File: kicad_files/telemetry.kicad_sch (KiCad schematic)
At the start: 24 parts, among them J5 SM10B-GHS-TB, J6 Conn_ARM_JTAG_SWD_10, J7 RFD900ux 3 Pin Power Select, J8 USB_C_Receptacle_USB2.0_16P, U8 74LVC1G125, U9 WE-TVS-82400102

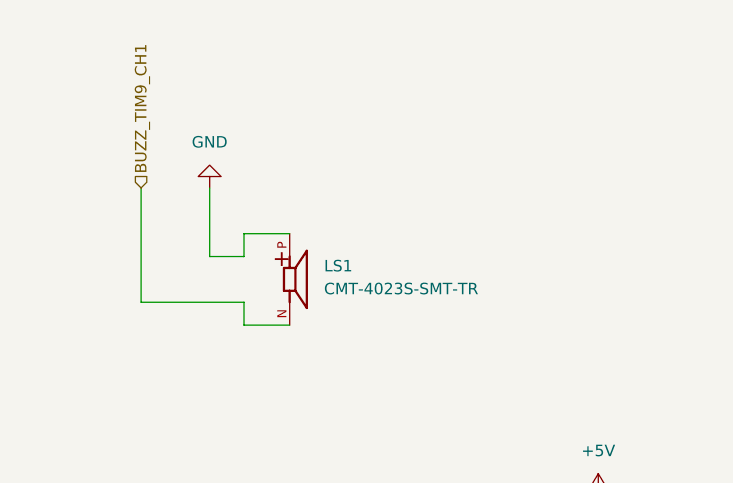
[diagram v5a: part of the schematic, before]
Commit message: fix buzzer
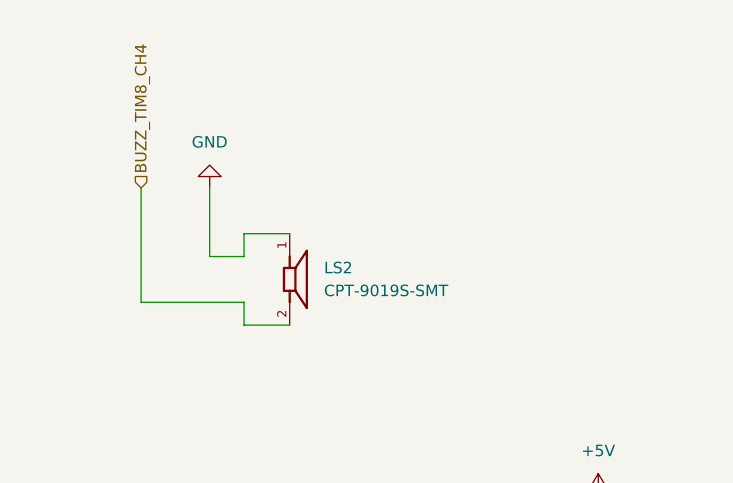
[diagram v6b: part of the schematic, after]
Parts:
- removed LS1: CMT-4023S-SMT-TR, footprints:CUI_CMT-4023S-SMT-TR, symbol CMT-4023S-SMT-TR:CMT-4023S-SMT-TR
- added LS2: CPT-9019S-SMT, footprints:CUI_CPT-9019S-SMT, symbol CPT-9019S-SMT:CPT-9019S-SMT
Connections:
- net GND: now also LS2.1
- new net BUZZ_TIM8_CH4: LS2.2
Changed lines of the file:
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@@
 		)
 	)
+	(hierarchical_label "BUZZ_TIM8_CH4"
+		(shape input)
+		(at 29.21 36.83 90)
+		(effects
+			(font
+				(size 1.27 1.27)
+			)
+			(justify left)
+		)
+	)
 	(hierarchical_label "RADIO_GPIO"
 		(shape input)
@@
 		)
 	)
-	(hierarchical_label "BUZZ_TIM9_CH1"
-		(shape input)
-		(at 29.21 36.83 90)
-		(effects
-			(font
-				(size 1.27 1.27)
-			)
-			(justify left)
-		)
-	)
 	(hierarchical_label "USART3_TX_RADIO"
 		(shape input)
@@
 	)
 	(symbol
+		(lib_id "CPT-9019S-SMT:CPT-9019S-SMT")
+		(at 45.72 46.99 0)
+		(unit 1)
+		(body_style 1)
+		(exclude_from_sim no)
+		(in_bom yes)
+		(on_board yes)
+		(in_pos_files yes)
+		(dnp no)
+		(fields_autoplaced yes)
+		(property "Reference" "LS2"
+			(at 49.53 45.7199 0)
+			(show_name no)
+			(do_not_autoplace no)
+			(effects
+				(font
+					(size 1.27 1.27)
+				)
+				(justify left)
+			)
+		)
+		(property "Value" "CPT-9019S-SMT"
+			(at 49.53 48.2599 0)
+			(show_name no)
+			(do_not_autoplace no)
+			(effects
+				(font
+					(size 1.27 1.27)
+				)
+				(justify left)
+			)
+		)
+		(property "Footprint" "footprints:CUI_CPT-9019S-SMT"
+			(at 45.72 46.99 0)
+			(hide yes)
+			(show_name no)
+			(do_not_autoplace no)
+			(effects
+				(font
+					(size 1.27 1.27)
+				)
+				(justify bottom)
+			)
+		)
+		(property "Datasheet" ""
+			(at 45.72 46.99 0)
+			(hide yes)
+			(show_name no)
+			(do_not_autoplace no)
+			(effects
+				(font
+					(size 1.27 1.27)
+				)
+			)
+		)
+		(property "Description" "9 mm, 25 Vp-p Vdc, 65 dB, Surface Mount (SMT), Piezo Audio Transducer Buzzer"
+			(at 45.72 46.99 0)
+			(hide yes)
+			(show_name no)
+			(do_not_autoplace no)
+			(effects
+				(font
+					(size 1.27 1.27)
+				)
+				(justify bottom)
+			)
+		)
+		(property "MF" "Same Sky"
+			(at 45.72 46.99 0)
+			(hide yes)
+			(show_name no)
+			(do_not_autoplace no)
+			(effects
+				(font
+					(size 1.27 1.27)
+				)
+				(justify bottom)
+			)
+		)
+		(property "Package" "None"
+			(at 45.72 46.99 0)
+			(hide yes)
+			(show_name no)
+			(do_not_autoplace no)
+			(effects
+				(font
+					(size 1.27 1.27)
+				)
+				(justify bottom)
+			)
+		)
+		(property "Price" "None"
+			(at 45.72 46.99 0)
+			(hide yes)
+			(show_name no)
+			(do_not_autoplace no)
+			(effects
+				(font
+					(size 1.27 1.27)
+				)
+				(justify bottom)
+			)
+		)
+		(property "Check_prices" "https://www.snapeda.com/parts/CPT-9019S-SMT-TR/Same+Sky/view-part/?ref=eda"
+			(at 45.72 46.99 0)
+			(hide yes)
+			(show_name no)
+			(do_not_autoplace no)
+			(effects
+				(font
+					(size 1.27 1.27)
+				)
+				(justify bottom)
+			)
+		)
+		(property "PART_REV" "1.0"
+			(at 45.72 46.99 0)
+			(hide yes)
+			(show_name no)
+			(do_not_autoplace no)
+			(effects
+				(font
+					(size 1.27 1.27)
+				)
+				(justify bottom)
+			)
+		)
+		(property "STANDARD" "MANUFACTURER RECOMMENDATIONS"
+			(at 45.72 46.99 0)
+			(hide yes)
+			(show_name no)
+			(do_not_autoplace no)
+			(effects
+				(font
+					(size 1.27 1.27)
+				)
+				(justify bottom)
+			)
+		)
+		(property "SnapEDA_Link" "https://www.snapeda.com/parts/CPT-9019S-SMT-TR/Same+Sky/view-part/?ref=snap"
+			(at 45.72 46.99 0)
+			(hide yes)
+			(show_name no)
+			(do_not_autoplace no)
+			(effects
+				(font
+					(size 1.27 1.27)
+				)
+				(justify bottom)
+			)
+		)
+		(property "MP" "CPT-9019S-SMT-TR"
+			(at 45.72 46.99 0)
+			(hide yes)
+			(show_name no)
+			(do_not_autoplace no)
+			(effects
+				(font
+					(size 1.27 1.27)
+				)
+				(justify bottom)
+			)
+		)
+		(property "Availability" "In Stock"
+			(at 45.72 46.99 0)
+			(hide yes)
+			(show_name no)
+			(do_not_autoplace no)
+			(effects
+				(font
+					(size 1.27 1.27)
+				)
+				(justify bottom)
+			)
+		)
+		(property "MANUFACTURER" "CUI INC"
+			(at 45.72 46.99 0)
+			(hide yes)
+			(show_name no)
+			(do_not_autoplace no)
+			(effects
+				(font
+					(size 1.27 1.27)
+				)
+				(justify bottom)
+			)
+		)
+		(pin "1"
+		)
+		(pin "2"
+		)
+		(instances
+			(project "versorlite"
+				(path "/1a230af0-0a74-48f7-8607-b087121dda49/4d884b5c-b332-4347-90a4-1c2e65497882"
+					(reference "LS2")
+					(unit 1)
+				)
+			)
+		)
+	)
+	(symbol
 		(lib_id "Connector:USB_C_Receptacle_USB2.0_16P")
 		(at 201.93 82.55 0)
@@
 					(unit 1)
 				)
-			)
-		)
-	)
-	(symbol
-		(lib_id "CMT-4023S-SMT-TR:CMT-4023S-SMT-TR")
-		(at 45.72 46.99 0)
-		(unit 1)
-		(body_style 1)
-		(exclude_from_sim no)
-		(in_bom yes)
-		(on_board yes)
-		(in_pos_files yes)
-		(dnp no)
-		(fields_autoplaced yes)
-		(property "Reference" "LS1"
-			(at 49.53 45.5097 0)
-			(show_name no)
-			(do_not_autoplace no)
-			(effects
-				(font
-					(size 1.27 1.27)
-				)
-				(justify left)
-			)
-		)
-		(property "Value" "CMT-4023S-SMT-TR"
-			(at 49.53 48.0497 0)
-			(show_name no)
-			(do_not_autoplace no)
-			(effects
-				(font
-					(size 1.27 1.27)
-				)
-				(justify left)
-			)
-		)
-		(property "Footprint" "footprints:CUI_CMT-4023S-SMT-TR"
-			(at 45.72 46.99 0)
-			(hide yes)
-			(show_name no)
-			(do_not_autoplace no)
-			(effects
-				(font
-					(size 1.27 1.27)
-				)
-				(justify bottom)
-			)
-		)
-		(property "Datasheet" ""
-			(at 45.72 46.99 0)
-			(hide yes)
-			(show_name no)
-			(do_not_autoplace no)
-			(effects
-				(font
-					(size 1.27 1.27)
-				)
-			)
-		)
-		(property "Description" "4 mm, 3 Vo-p, 70 dB, Surface Mount (SMT), Magnetic Audio Transducer Buzzer"
-			(at 45.72 46.99 0)
-			(hide yes)
-			(show_name no)
-			(do_not_autoplace no)
-			(effects
-				(font
-					(size 1.27 1.27)
-				)
-				(justify bottom)
-			)
-		)
-		(property "MF" "Same Sky"
-			(at 45.72 46.99 0)
-			(hide yes)
-			(show_name no)
-			(do_not_autoplace no)
-			(effects
-				(font
-					(size 1.27 1.27)
-				)
-				(justify bottom)
-			)
-		)
-		(property "Package" "None"
-			(at 45.72 46.99 0)
-			(hide yes)
-			(show_name no)
-			(do_not_autoplace no)
-			(effects
-				(font
-					(size 1.27 1.27)
-				)
-				(justify bottom)
-			)
-		)
-		(property "Price" "None"
-			(at 45.72 46.99 0)
-			(hide yes)
-			(show_name no)
-			(do_not_autoplace no)
-			(effects
-				(font
-					(size 1.27 1.27)
-				)
-				(justify bottom)
-			)
-		)
-		(property "Check_prices" "https://www.snapeda.com/parts/CMT-4023S-SMT-TR/Same+Sky/view-part/?ref=eda"
-			(at 45.72 46.99 0)
-			(hide yes)
-			(show_name no)
-			(do_not_autoplace no)
-			(effects
-				(font
-					(size 1.27 1.27)
-				)
-				(justify bottom)
-			)
-		)
-		(property "STANDARD" "Manufacturer recommendations"
-			(at 45.72 46.99 0)
-			(hide yes)
-			(show_name no)
-			(do_not_autoplace no)
-			(effects
-				(font
-					(size 1.27 1.27)
-				)
-				(justify bottom)
-			)
-		)
-		(property "PARTREV" "1.0"
-			(at 45.72 46.99 0)
-			(hide yes)
-			(show_name no)
-			(do_not_autoplace no)
-			(effects
-				(font
-					(size 1.27 1.27)
-				)
-				(justify bottom)
-			)
-		)
-		(property "SnapEDA_Link" "https://www.snapeda.com/parts/CMT-4023S-SMT-TR/Same+Sky/view-part/?ref=snap"
-			(at 45.72 46.99 0)
-			(hide yes)
-			(show_name no)
-			(do_not_autoplace no)
-			(effects
-				(font
-					(size 1.27 1.27)
-				)
-				(justify bottom)
-			)
-		)
-		(property "MP" "CMT-4023S-SMT-TR"
-			(at 45.72 46.99 0)
-			(hide yes)
-			(show_name no)
-			(do_not_autoplace no)
-			(effects
-				(font
-					(size 1.27 1.27)
-				)
-				(justify bottom)
-			)
-		)
-		(property "Availability" "In Stock"
-			(at 45.72 46.99 0)
-			(hide yes)
-			(show_name no)
-			(do_not_autoplace no)
-			(effects
-				(font
-					(size 1.27 1.27)
-				)
-				(justify bottom)
-			)
-		)
-		(property "MANUFACTURER" "CUI INC"
-			(at 45.72 46.99 0)
-			(hide yes)
-			(show_name no)
-			(do_not_autoplace no)
-			(effects
-				(font
-					(size 1.27 1.27)
-				)
-				(justify bottom)
-			)
-		)
-		(pin "P"
-		)
-		(pin "N"
-		)
-		(instances
-			(project "versorlite"
-				(path "/1a230af0-0a74-48f7-8607-b087121dda49/4d884b5c-b332-4347-90a4-1c2e65497882"
-					(reference "LS1")
-					(unit 1)
-				)

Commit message: update
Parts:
- D5: value PMEG6045ETPX -> SS54; footprint Diode_SMD:D_SOD-128 -> Diode_SMD:D_SMA
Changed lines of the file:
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@@
 			)
 		)
-		(property "Value" "PMEG6045ETPX"
+		(property "Value" "SS54"
 			(at 241.554 36.576 90)
 			(show_name no)
@@
 			)
 		)
-		(property "Footprint" "Diode_SMD:D_SOD-128"
+		(property "Footprint" "Diode_SMD:D_SMA"
 			(at 238.76 36.83 90)
 			(hide yes)

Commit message: jlcpcb fixes
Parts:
- removed R13, R14: 22ohm, Resistor_SMD:R_0402_1005Metric, symbol Device:R_US
- removed U9: WE-TVS-82400102, Package_TO_SOT_SMD:SOT-23-6, symbol Power_Protection:WE-TVS-82400102
- added U11: PESD2USB5UX, Package_TO_SOT_SMD:TSOT-23, symbol Power_Management:PESD2USB5UX
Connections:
- net D+: now also J8.A6 (D+), J8.B6 (D+), U11.2
- net D-: now also J8.A7 (D-), J8.B7 (D-), U11.1
- net GND: now also U11.3
